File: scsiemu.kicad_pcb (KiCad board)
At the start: 2 copper layers, 100 x 99 mm, 56 parts, among them J1 RasPi, J2 SCSI, J3 USB_POWER, J4 POWER 5V, J5 POWER 5V, J6 AT Power 5V (171826-4), J7 I2C Ext, J8 AT Power 5V (641737-1), U1 74LS641-1, U2 74LS641-1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

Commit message: minor update
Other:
- board text added: "SCSI emu v2.1"
- board text removed: "SCSI emu v2"

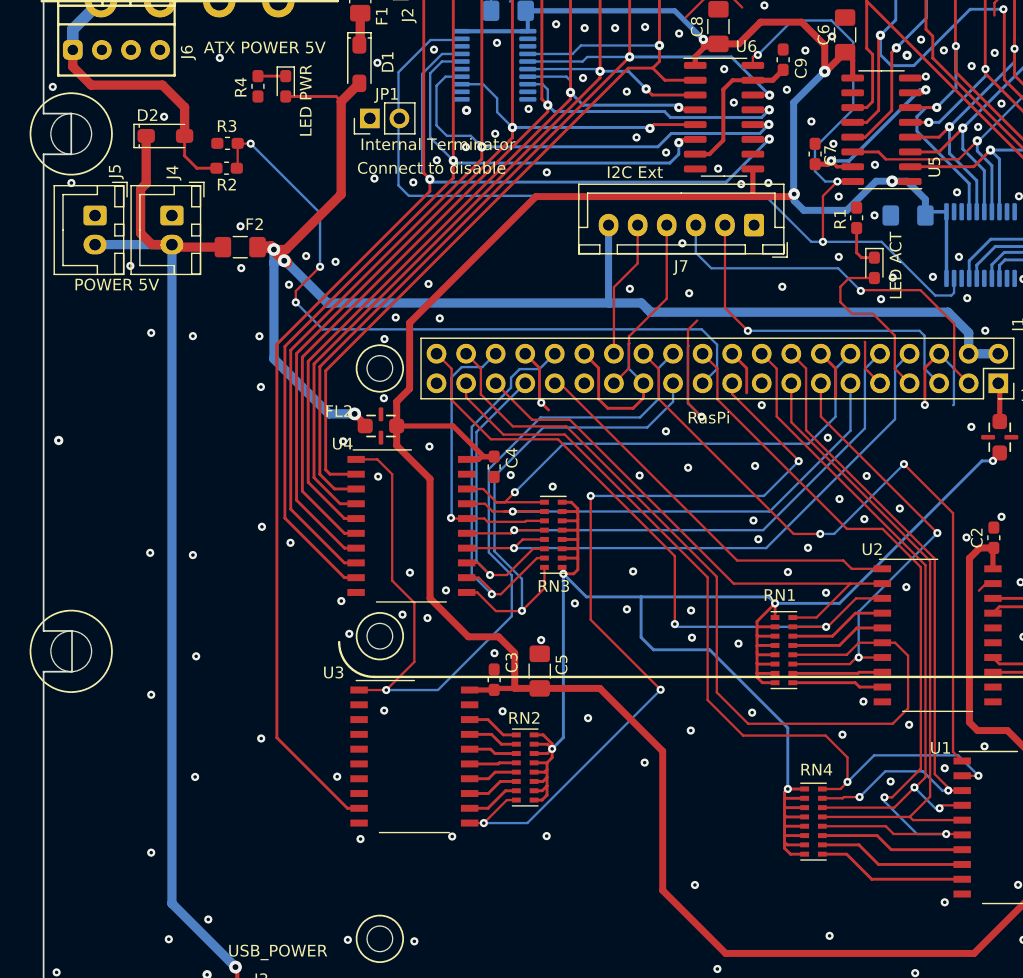
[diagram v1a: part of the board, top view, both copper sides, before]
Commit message: add auto power off
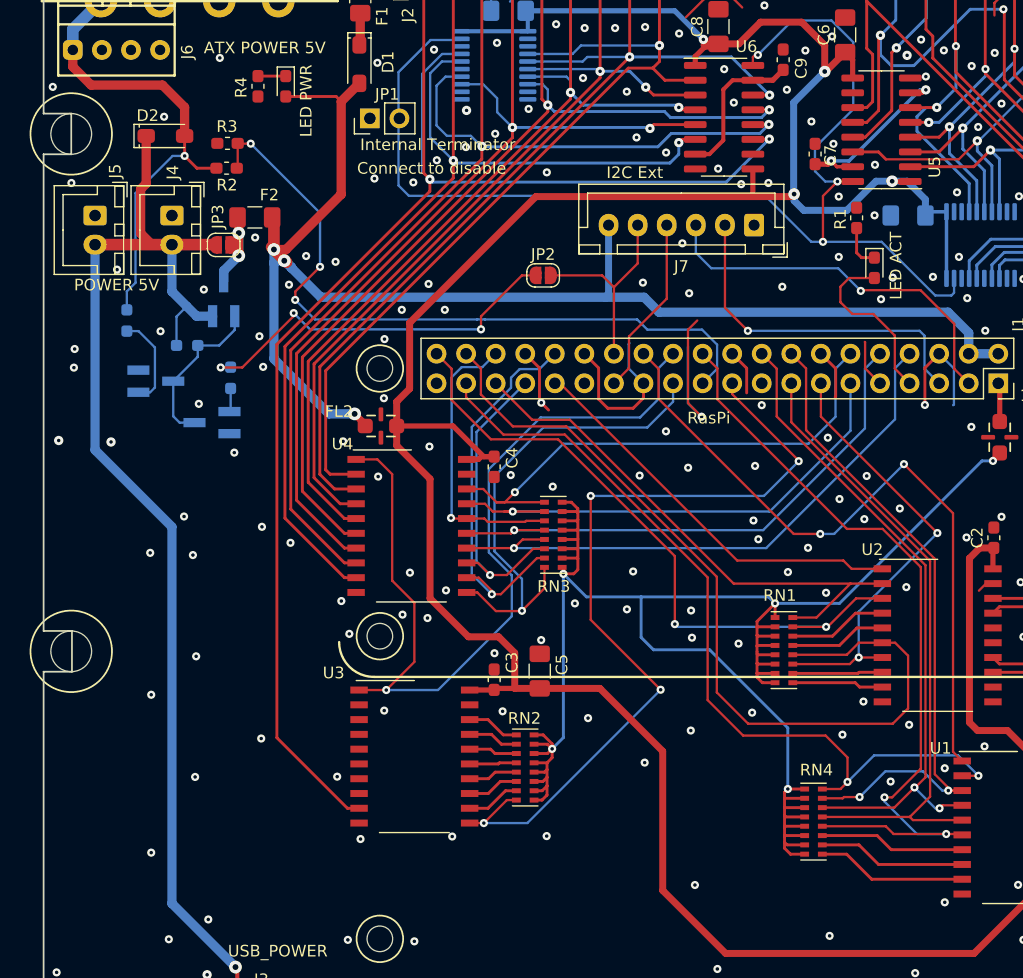
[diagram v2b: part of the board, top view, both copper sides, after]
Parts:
- added JP2: Use Raspi Power Off, Jumper:SolderJumper-2_P1.3mm_Open_RoundedPad1.0x1.5mm, F.Cu at (152.5, 69.2)
- added JP3: Power No Switch JMP, Jumper:SolderJumper-2_P1.3mm_Open_RoundedPad1.0x1.5mm, F.Cu at (125.1, 66.5)
- added Q1: DMG3415U, Package_TO_SOT_SMD:SOT-23_Handsoldering, B.Cu at (125.1, 71.2)
- added Q2: 2SC2712, Package_TO_SOT_SMD:SOT-23_Handsoldering, B.Cu at (119.3, 78.2)
- added Q3: 2SC2712, Package_TO_SOT_SMD:SOT-23_Handsoldering, B.Cu at (124.1, 81.8)
- added R5: 47k, Resistor_SMD:R_0603_1608Metric_Pad0.98x0.95mm_HandSolder, B.Cu at (122.0, 75.2)
- added R6: 10k, Resistor_SMD:R_0603_1608Metric_Pad0.98x0.95mm_HandSolder, B.Cu at (116.8, 73.0)
- added R7: 10k, Resistor_SMD:R_0603_1608Metric_Pad0.98x0.95mm_HandSolder, B.Cu at (125.7, 78.0)
- moved F2 2.85 mm to (127.8, 64.2)
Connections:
- F2 pad 2: Net-(D2-Pad1) -> Net-(F2-Pad2)
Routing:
- net Net-(JP2-Pad1): track 0.00 -> 33.1 mm, vias 0 -> 3
- net /AT_5V_DC: track 25.0 -> 40.9 mm, vias 0 -> 1
- net Net-(D2-Pad1): track 90.8 -> 105.3 mm
- net Net-(Q1-Pad1): track 0.00 -> 13.9 mm
- net Net-(F2-Pad2): track 0.00 -> 9.04 mm, vias 0 -> 2
- net Net-(Q2-Pad1): track 0.00 -> 8.02 mm
- net /EXT2: track 11.9 -> 17.7 mm
- net /5V_DC: track 120.3 -> 122.5 mm
- net Net-(Q3-Pad1): track 0.00 -> 2.03 mm
- net GND: vias 196 -> 201
